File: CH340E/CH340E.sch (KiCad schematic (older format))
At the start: 18 parts, among them J2 Conn_01x06, P1 USB_C_Plug_USB2.0, U1 CH340E, U2 AP2127K-3.3

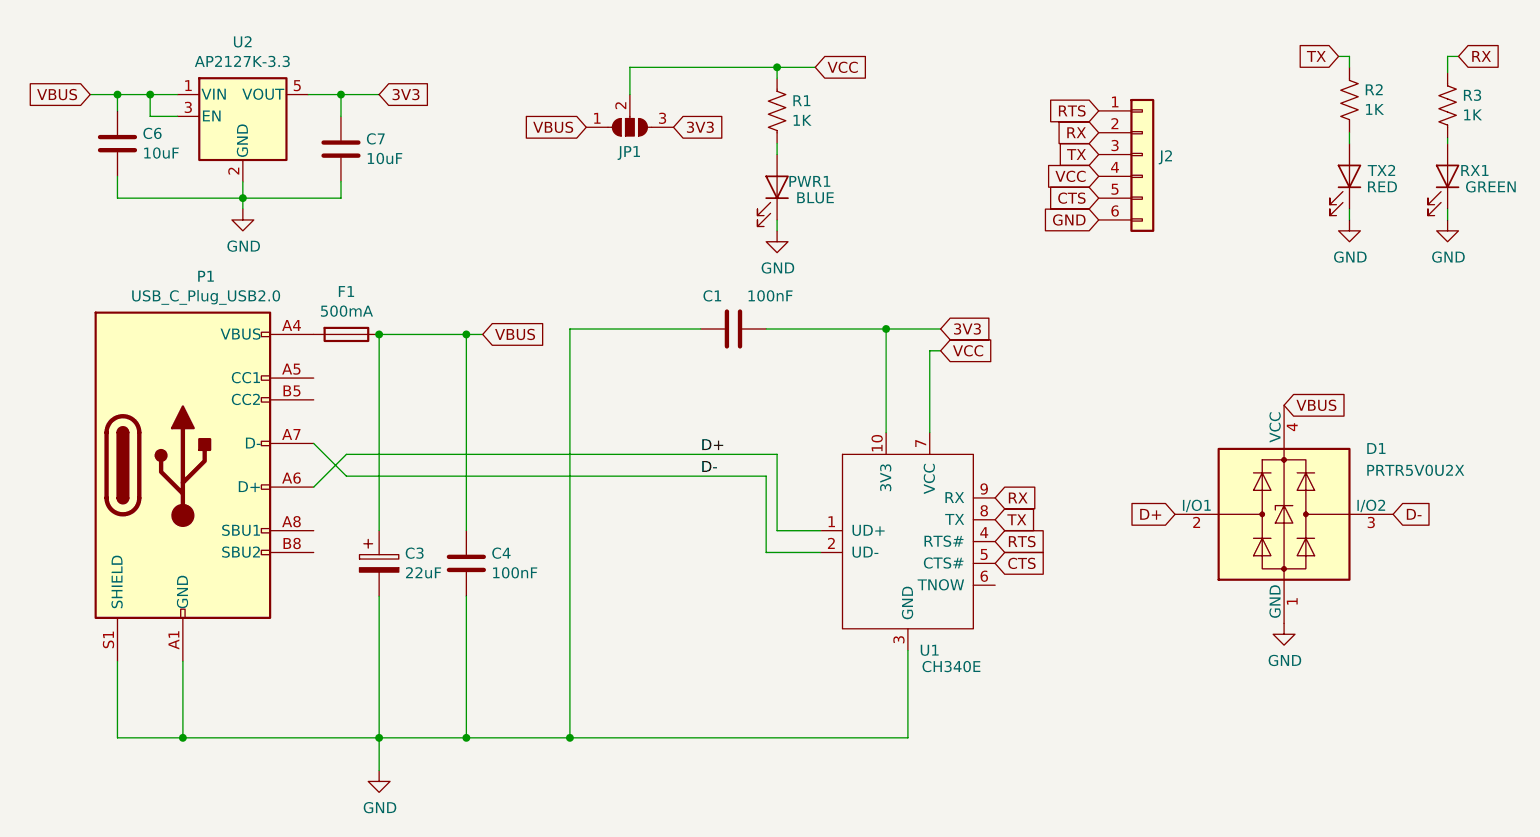
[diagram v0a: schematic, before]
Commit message: CH340E Fix
5k1 Resistors added to CC1 and CC2, TX and RX LEDs pulled up to VCC,Copper Pour changed from 3V3 to VCC.
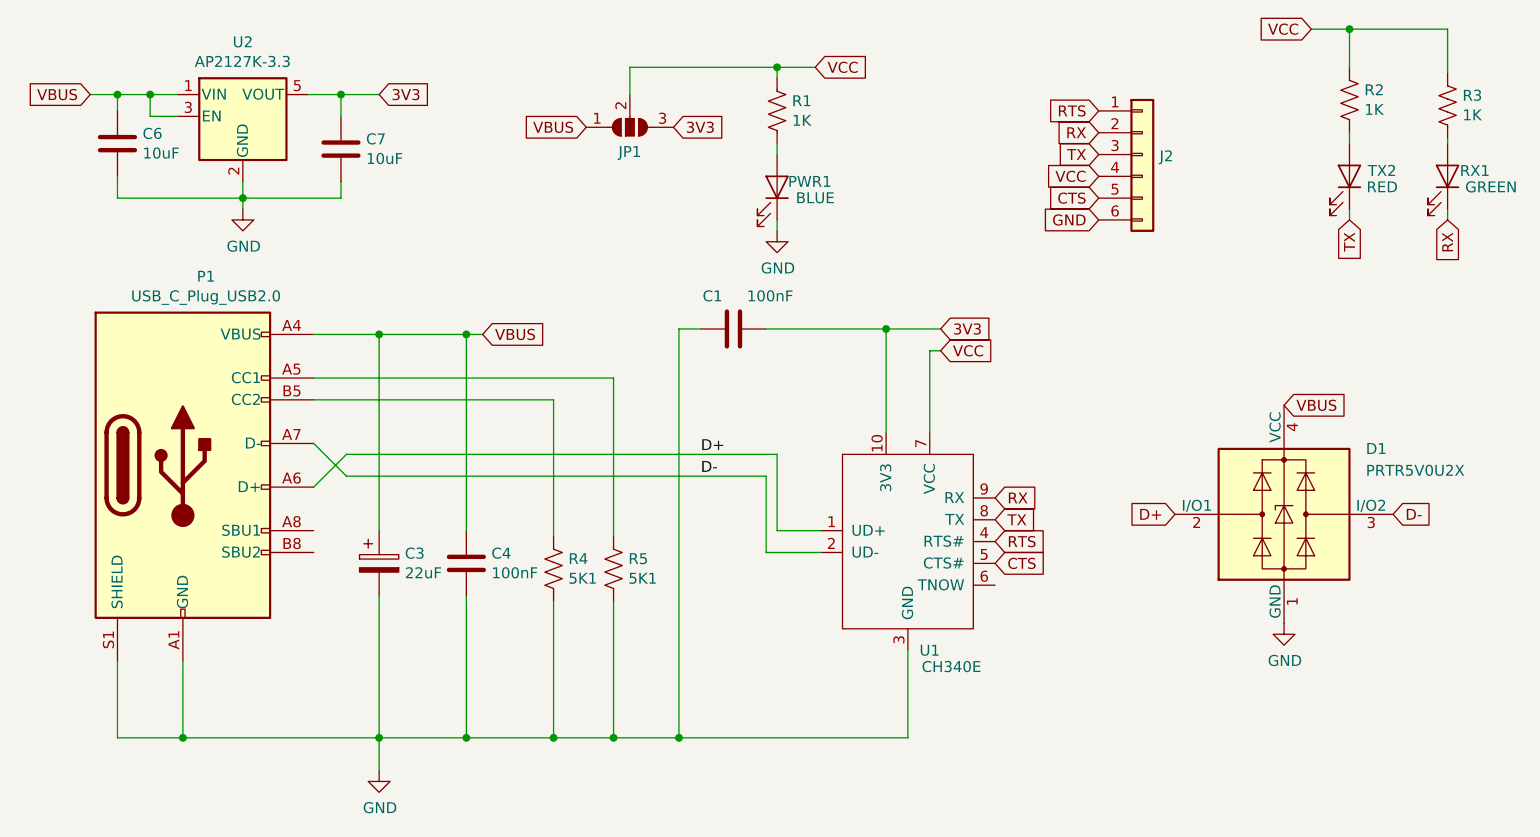
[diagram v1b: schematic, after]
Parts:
- removed F1: 500mA, Resistor_SMD:R_0805_2012Metric, symbol Device:Fuse
- added R4, R5: 5K1, Resistor_SMD:R_0603_1608Metric, symbol Device:R_US
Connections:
- net GND: now also R4.2, R5.2; no longer RX1.1 (K), TX2.1 (K)
- net RX: now also RX1.1 (K); no longer R3.1
- net TX: now also TX2.1 (K); no longer R2.1
- net VBUS: now also P1.A4 (VBUS), P1.A9 (VBUS), P1.B4 (VBUS), P1.B9 (VBUS)
- net VCC: now also R2.1, R3.1
- net at P1.A5 (CC1): now also R5.1
- net at P1.B5 (CC2): now also R4.1
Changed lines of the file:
@@
 	4675 2025 4675 2500
 Wire Wire Line
-	3825 2025 3225 2025
+	3825 2025 3725 2025
 Text GLabel 5175 3100 2    50   Input ~ 0
 CTS
@@
 Wire Wire Line
 	7250 1175 7250 1150
-$Comp
-L power:GND #PWR0103
-U 1 1 5E4C8EE3
-P 7250 1525
-F 0 "#PWR0103" H 7250 1275 50  0001 C CNN
-F 1 "GND" H 7254 1353 50  0000 C CNN
-F 2 "" H 7250 1525 50  0001 C CNN
-F 3 "" H 7250 1525 50  0001 C CNN
-	1    7250 1525
-	1    0    0    -1
-$EndComp
 Wire Wire Line
 	7250 1525 7250 1475
@@
 	1    0    0    -1
 $EndComp
-Text GLabel 7300 775  2    50   Input ~ 0
+Text GLabel 7250 1525 3    50   Input ~ 0
 RX
-Wire Wire Line
-	7300 775  7250 775
-Wire Wire Line
-	7250 775  7250 850
-Text GLabel 6750 775  0    50   Input ~ 0
+Text GLabel 6800 1525 3    50   Input ~ 0
 TX
-Wire Wire Line
-	6750 775  6800 775
 $Comp
 L Device:LED RX1
@@
 Wire Wire Line
 	6800 1525 6800 1475
-$Comp
-L power:GND #PWR0104
-U 1 1 5E4E74AC
-P 6800 1525
-F 0 "#PWR0104" H 6800 1275 50  0001 C CNN
-F 1 "GND" H 6804 1353 50  0000 C CNN
-F 2 "" H 6800 1525 50  0001 C CNN
-F 3 "" H 6800 1525 50  0001 C CNN
-	1    6800 1525
-	1    0    0    -1
-$EndComp
-Wire Wire Line
-	6800 825  6800 775
 Wire Wire Line
 	6800 1175 6800 1125
@@
 	4175 825  4350 825
 $Comp
-L Device:Fuse F1
-U 1 1 5E50B6C1
-P 2200 2050
-F 0 "F1" V 2005 2050 50  0000 C CNN
-F 1 "500mA" V 2095 2050 50  0000 C CNN
-F 2 "Resistor_SMD:R_0805_2012Metric" V 2130 2050 50  0001 C CNN
-F 3 "~" H 2200 2050 50  0001 C CNN
-F 4 "C89657" V 2200 2050 50  0001 C CNN "Part"
-	1    2200 2050
-	0    1    1    0
-$EndComp
-Connection ~ 2350 2050
-$Comp
 L Power_Protection:PRTR5V0U2X D1
 U 1 1 5E5751C6
@@
 	1    0    0    -1
 $EndComp
-Connection ~ 3225 3900
-Wire Wire Line
-	3225 2025 3225 3900
-Wire Wire Line
-	3225 3900 4775 3900
+Connection ~ 3725 3900
+Wire Wire Line
+	3725 2025 3725 3900
+Wire Wire Line
+	3725 3900 4775 3900
 Connection ~ 2750 2050
 Connection ~ 2750 3900
 Wire Wire Line
-	2750 3900 3225 3900
+	2750 3900 3150 3900
 Wire Wire Line
 	2350 2050 2750 2050
@@
 	0    -1   -1   0
 $EndComp
+Text GLabel 6625 650  0    50   Input ~ 0
+VCC
+Wire Wire Line
+	7250 850  7250 650
+Wire Wire Line
+	6625 650  6800 650
+Wire Wire Line
+	6800 650  6800 825
+Connection ~ 6800 650
+Wire Wire Line
+	6800 650  7250 650
+$Comp
+L Device:R_US R4
+U 1 1 5E97E6A1
+P 3150 3125
+F 0 "R4" H 3218 3170 50  0000 L CNN
+F 1 "5K1" H 3218 3080 50  0000 L CNN
+F 2 "Resistor_SMD:R_0603_1608Metric" V 3190 3115 50  0001 C CNN
+F 3 "~" H 3150 3125 50  0001 C CNN
+F 4 "C332117" H 3150 3125 50  0001 C CNN "Part"
+	1    3150 3125
+	1    0    0    -1
+$EndComp
+$Comp
+L Device:R_US R5
+U 1 1 5E98016F
+P 3425 3125
+F 0 "R5" H 3493 3170 50  0000 L CNN
+F 1 "5K1" H 3493 3080 50  0000 L CNN
+F 2 "Resistor_SMD:R_0603_1608Metric" V 3465 3115 50  0001 C CNN
+F 3 "~" H 3425 3125 50  0001 C CNN
+F 4 "C332117" H 3425 3125 50  0001 C CNN "Part"
+	1    3425 3125
+	1    0    0    -1
+$EndComp
+Wire Wire Line
+	2050 2350 3150 2350
+Wire Wire Line
+	3150 2350 3150 2975
+Wire Wire Line
+	2050 2250 3425 2250
+Wire Wire Line
+	3425 2250 3425 2975
+Wire Wire Line
+	3150 3275 3150 3900
+Connection ~ 3150 3900
+Wire Wire Line
+	3150 3900 3425 3900
+Wire Wire Line
+	3425 3275 3425 3900
+Connection ~ 3425 3900
+Wire Wire Line
+	3425 3900 3725 3900
+Wire Wire Line
+	2050 2050 2350 2050
+Connection ~ 2350 2050
 $EndSCHEMATC
